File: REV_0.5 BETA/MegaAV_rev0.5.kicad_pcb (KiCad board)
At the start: 4 copper layers, 50 x 50 mm, 166 parts, among them CN1 MD-90SM_MD2, P1 SMD_Conn_01x01, U1 4070, U2 74HC123, U3 TS924, U4 THS7374, U5 ICS501, U6 TS922, U7 TS924, U8 AD725

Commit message: Replace Mega AV Logo with current one
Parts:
- removed the G*** at (182.4, 128.9)
- added G***: LOGO, LOGO_Library:MegaAV Logo (med), B.Cu at (185.2, 127.0)

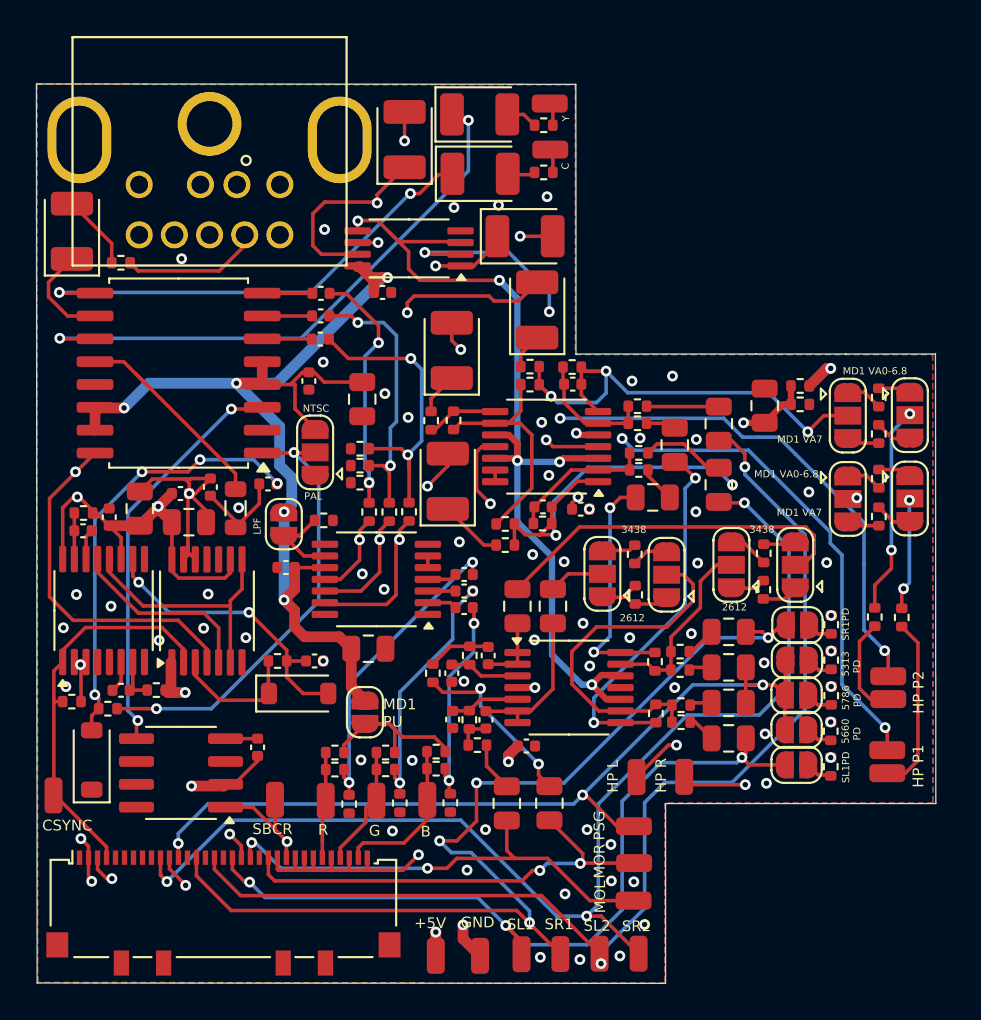
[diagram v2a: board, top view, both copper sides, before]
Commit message: Added SL3 and SR3 (Sega CD passthrough)
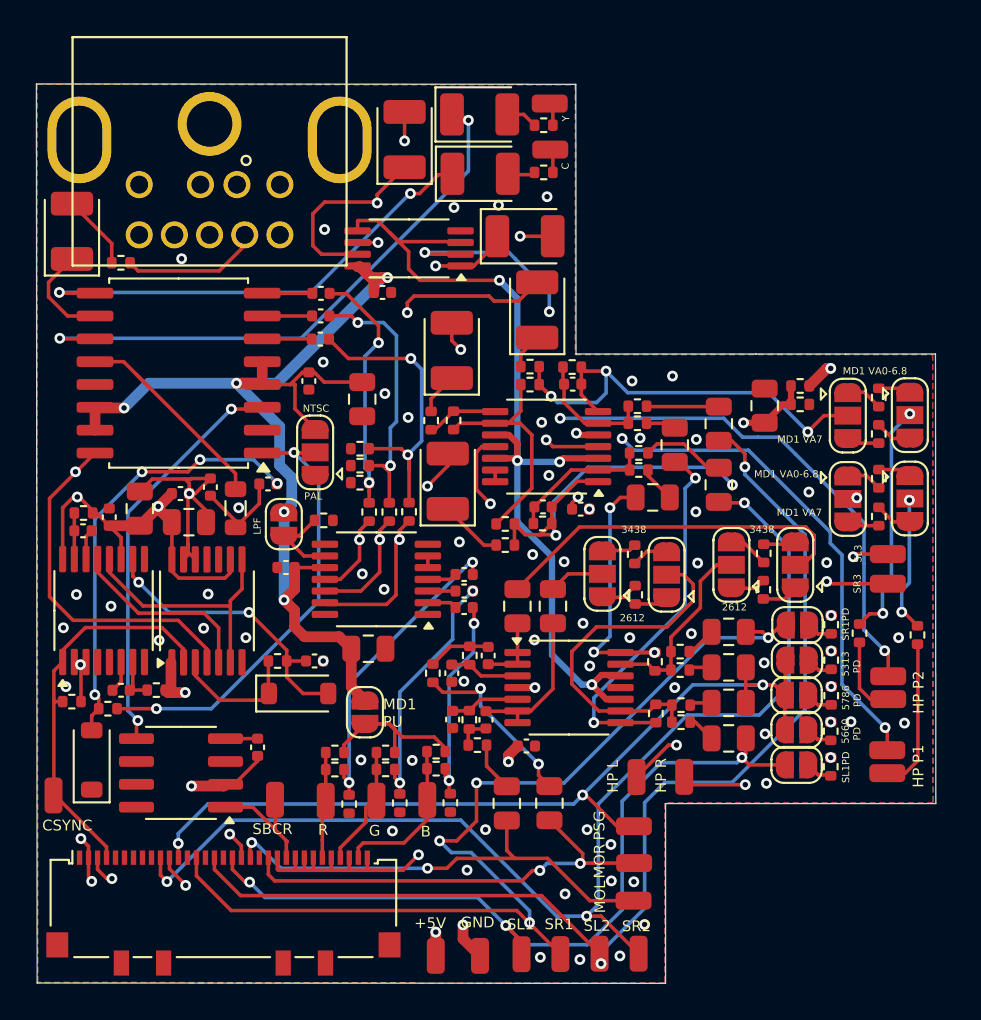
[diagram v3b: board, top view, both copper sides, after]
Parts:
- added SL3: SMD_Conn_01x01, Connector_Wire:SolderWirePad_1x01_SMD_1x2mm, F.Cu at (216.7, 120.5)
- added SR3: SMD_Conn_01x01, Connector_Wire:SolderWirePad_1x01_SMD_1x2mm, F.Cu at (216.7, 122.1)
- moved R60 1.31 mm to (218.3, 125.0)
- moved R61 1.24 mm to (215.1, 124.9)
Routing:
- net Net-(SR3-Pin_1): track 13.5 -> 30.0 mm, vias 2 -> 4
- net Net-(SL3-Pin_1): track 20.9 -> 33.8 mm, vias 2 -> 3
- net Net-(HPL_RES2-C): track 45.8 -> 47.5 mm
- net Net-(HPR_RES2-C): track 52.8 -> 54.3 mm
- net Net-(HPR_SL1-Pin_1): track 9.81 -> 8.54 mm
- net Net-(HPL_SL1-Pin_1): track 5.65 -> 4.45 mm
- net GND: vias 69 -> 72
- net /V_REF: vias 7 -> 6
- net /CLK: vias 1 -> 0

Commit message: Silkscreen improvments
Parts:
- renumbered SL3 to CDL, SR3 to CDR
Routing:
- net GND: vias 72 -> 67
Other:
- board text added: "32x L"
- board text added: "32x R"
- board text added: "CDL"
- board text added: "CDR"
- board text added: "FML"
- board text added: "FMR"
- board text added: "JUMPER SETTINGS: MD1 VA0-VA6.8: 5313 PD, 2612 MD1 VA7, MD2 VA3-VA4 5660 PD, 3438 MD2 VA0-VA1.8, MD3: 5660 PD, 3438, SL1 PD, SR1 PD MD2 VA2-VA2.3 5786 PD, 2612 PAL: PAL, NTSC: NTSC LIFTED RGB: MD1PU"
- board text added: "MD1 PD"
- board text added: "MD2 VA0-1.8/MD3"
- board text added: "MD2* MD3 PD"
- board text added: "Pass"
- board text added: "T PD"
- board text removed: "5313 PD"
- board text removed: "5660 PD"
- board text removed: "5786 PD"
- board text removed: "JUMPER SETTINGS: MD1 VA0-VA6.8: 5313 PD, 2612 MD1 VA7, MD2 VA3-VA4 5660 PD, 3438 MD2 VA0-VA1.8, MD3: 5660 PD, 3438, SL1 PD, SR1 PD MD2 VA2-VA2.3 5786 PD, 2612 MD3 VA1: 5660 PD, 3438 MD3 VA2: 5660 PD, 3438 PAL: PAL, NTSC: NTSC LIFTED RGB: MD1PU"
- board text removed: "MOL"
- board text removed: "MOR"
- board text removed: "SL1"
- board text removed: "SL1PD"
- board text removed: "SL2"
- board text removed: "SR1"
- board text removed: "SR1PD"
- board text removed: "SR2"

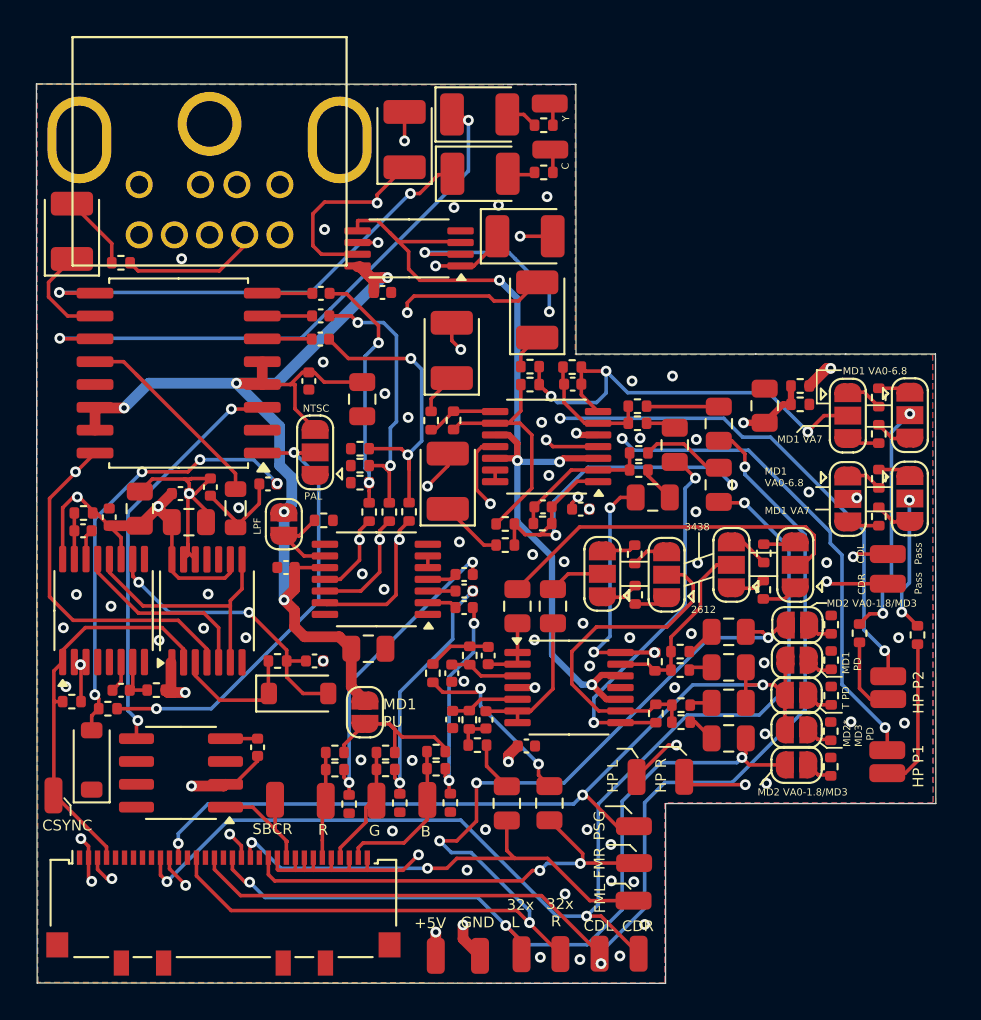
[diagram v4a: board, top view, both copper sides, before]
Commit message: 74HC86 support + silkscreening improvments.
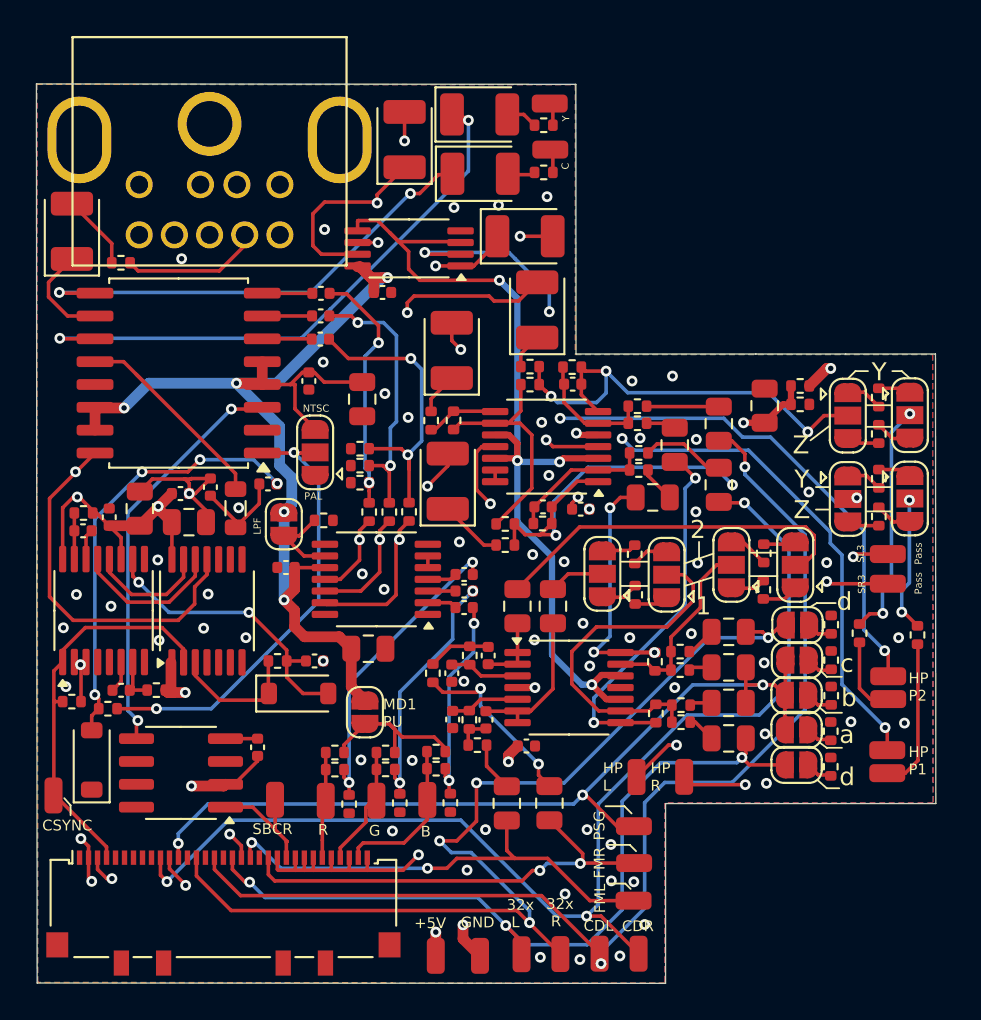
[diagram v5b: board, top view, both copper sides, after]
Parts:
- removed the G*** at (185.2, 127.0)
- added G***: LOGO, LOGO_Library:MegaAV Logo 2, B.Cu at (182.4, 122.5)
- moved G*** 36.0 mm to (193.2, 141.0), turned to 90 degrees
- renumbered CDL to SL3, CDR to SR3
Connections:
- U1 pad 10: /Vsync -> GND
- U1 pad 11: unconnected-(U1-Pad11) -> /CSync_OUT
- U1 pad 12: GND -> /Hsync
- U1 pad 13: GND -> /~Vsync
- U1 pad 4: /CSync_OUT -> GND
- U1 pad 5: /Hsync -> GND
- U1 pad 6: /~Vsync -> GND
- U1 pad 8: /~Vsync -> GND
- U1 pad 9: +5V -> GND
- U2 pad 5: unconnected-(U2B-Q-Pad5) -> /Vsync
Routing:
- net /~Vsync: track 14.2 -> 6.76 mm
- net +5V: track 258.0 -> 253.1 mm
- net GND: track 40.6 -> 35.9 mm, vias 67 -> 68
- net /Hsync: track 10.7 -> 8.38 mm
- net /CSync_OUT: track 37.1 -> 38.1 mm
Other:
- board text added: "1"
- board text added: "2"
- board text added: "JUMPER SETTINGS: MD1 VA0-VA6.8: c, 1 MD1 VA7, MD2 VA3-VA4: a, 2 MD2 VA0-VA1.8/MD3: a, d, 2 MD2 VA2-VA2.3 b, 1 REGION SELECT: Bridge PAL Or NTSC Jumper If you LIFTED RGB Legs: MD1PU HEADPHONE OUT: MD1 VA0-VA6.8: Y MD1 VA7, CDX, NOMAD, MEGA JET: Z NO HEADPHONE OUT: MD1 VA7: SHORT HP P1 AND HP P2"
- board text added: "Z"
- board text added: "a"
- board text added: "b"
- board text added: "c"
- board text added: "d"
- board text removed: "2612"
- board text removed: "3438"
- board text removed: "HEADPHONE OUT: MD1 VA0-VA6.8: VA0-6.8 MD1 VA7, CDX, NOMAD, MEGA JET: VA7 NO HEADPHONE OUT: VA7, SHORT HP P1 AND HP P2"
- board text removed: "JUMPER SETTINGS: MD1 VA0-VA6.8: 5313 PD, 2612 MD1 VA7, MD2 VA3-VA4 5660 PD, 3438 MD2 VA0-VA1.8, MD3: 5660 PD, 3438, SL1 PD, SR1 PD MD2 VA2-VA2.3 5786 PD, 2612 PAL: PAL, NTSC: NTSC LIFTED RGB: MD1PU"
- board text removed: "MD1 PD"
- board text removed: "MD1 VA0-6.8"
- board text removed: "MD1 VA7"
- board text removed: "MD2 VA0-1.8/MD3"
- board text removed: "MD2* MD3 PD"
- board text removed: "T PD"

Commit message: added 10k pullup to HCT123, silkscreening improvments, GND pad next to SBCR
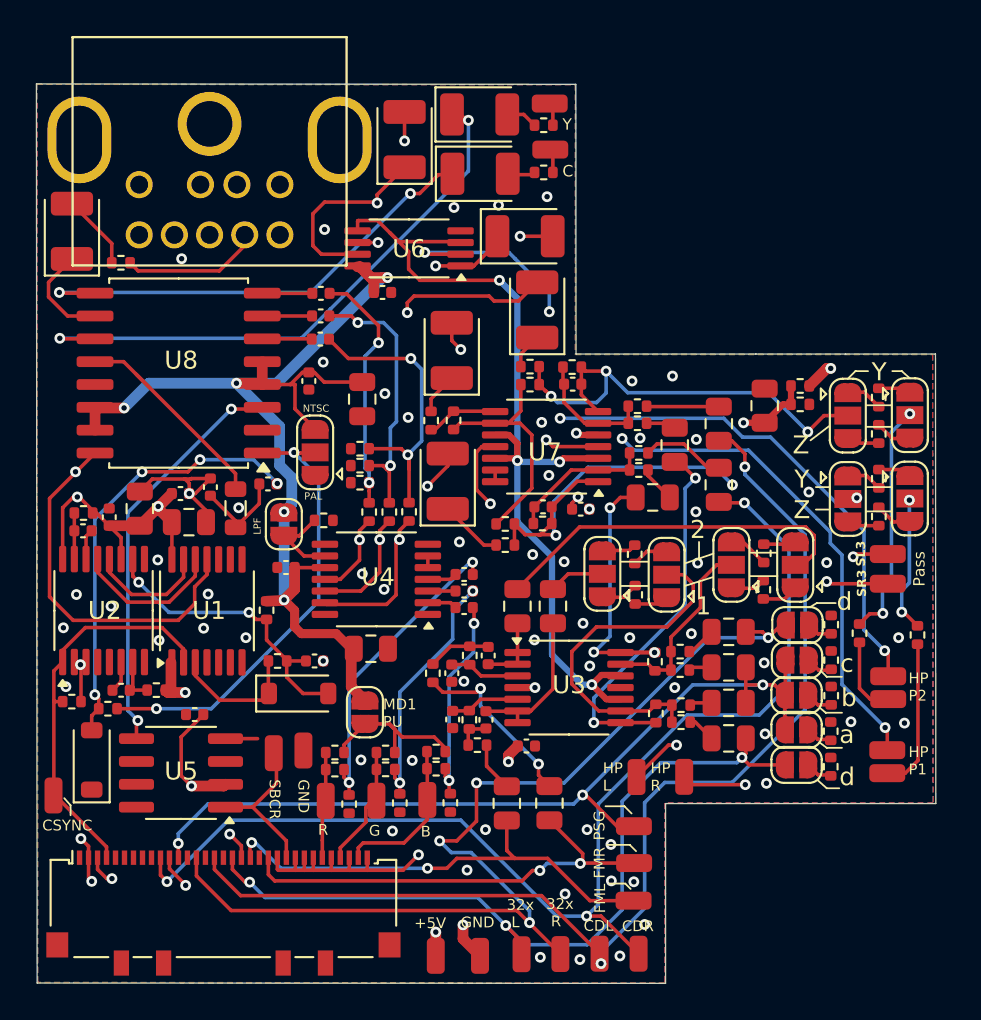
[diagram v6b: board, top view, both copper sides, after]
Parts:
- added ?: , , F.Cu at (184.2, 131.4)
- added R20: 10k, Resistor_SMD:R_0402_1005Metric, F.Cu at (182.1, 123.6)
- U2: value 74HC123 -> 74HCT123
- moved C23 3.94 mm to (178.1, 129.4), turned to 0 degrees
- moved CLK_IN1 2.59 mm to (182.5, 131.6)
- moved C29 0.14 mm to (187.9, 125.7)
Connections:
- Z1 pad MP: GND -> (no net)
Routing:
- net +5V: track 253.1 -> 255.7 mm
- net /CLK: track 6.95 -> 8.71 mm
